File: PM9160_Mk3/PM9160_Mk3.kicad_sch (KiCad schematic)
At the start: 87 parts, among them J1 Conn_Coaxial, U1 BGA2869, U2 ATtiny416-M, U3 SY100EL33L, U4 SY100EL33L, U5 LM317L_TO92

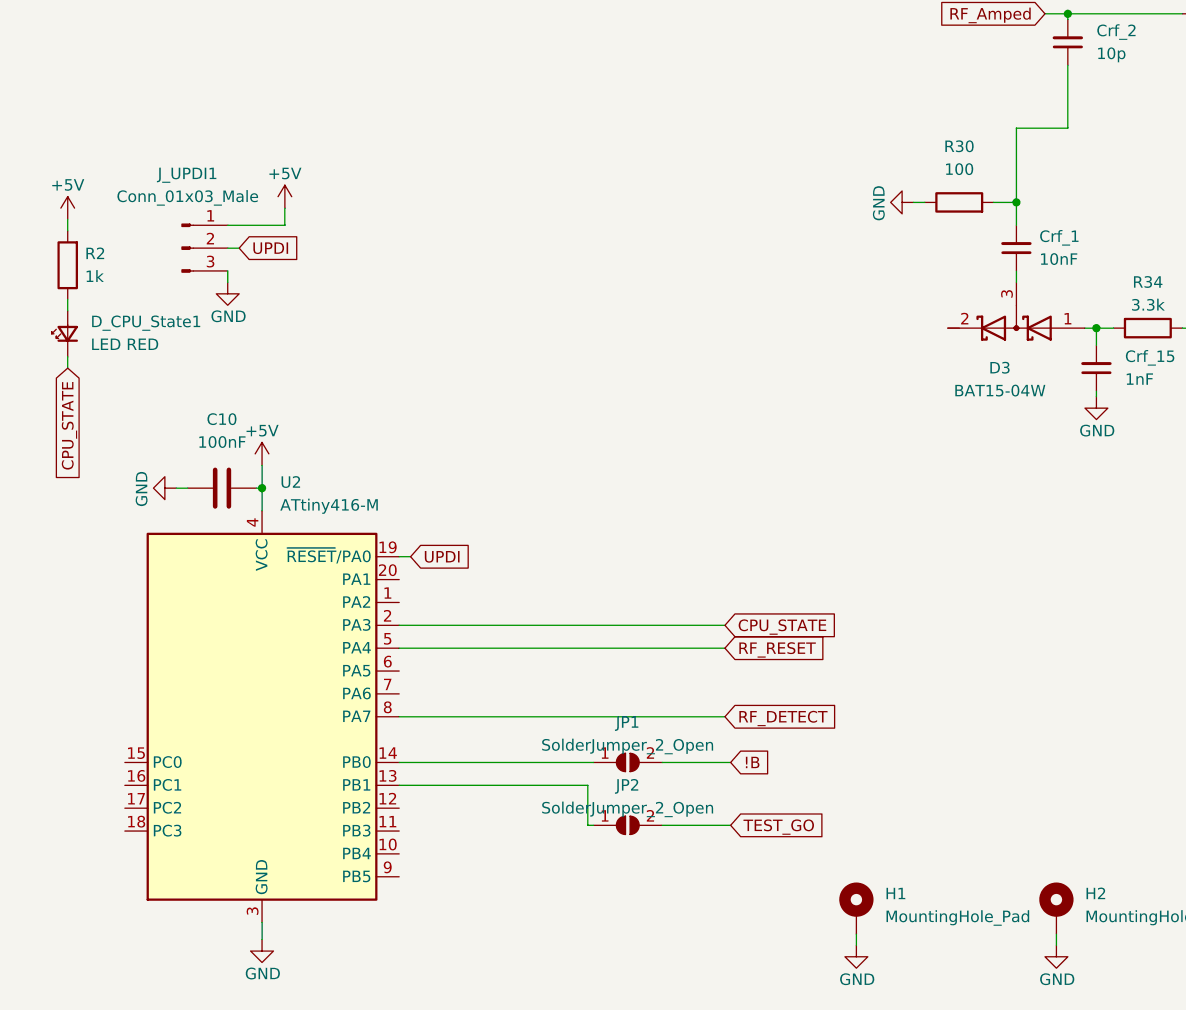
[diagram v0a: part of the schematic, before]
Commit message: CPU change and fixed via clearances
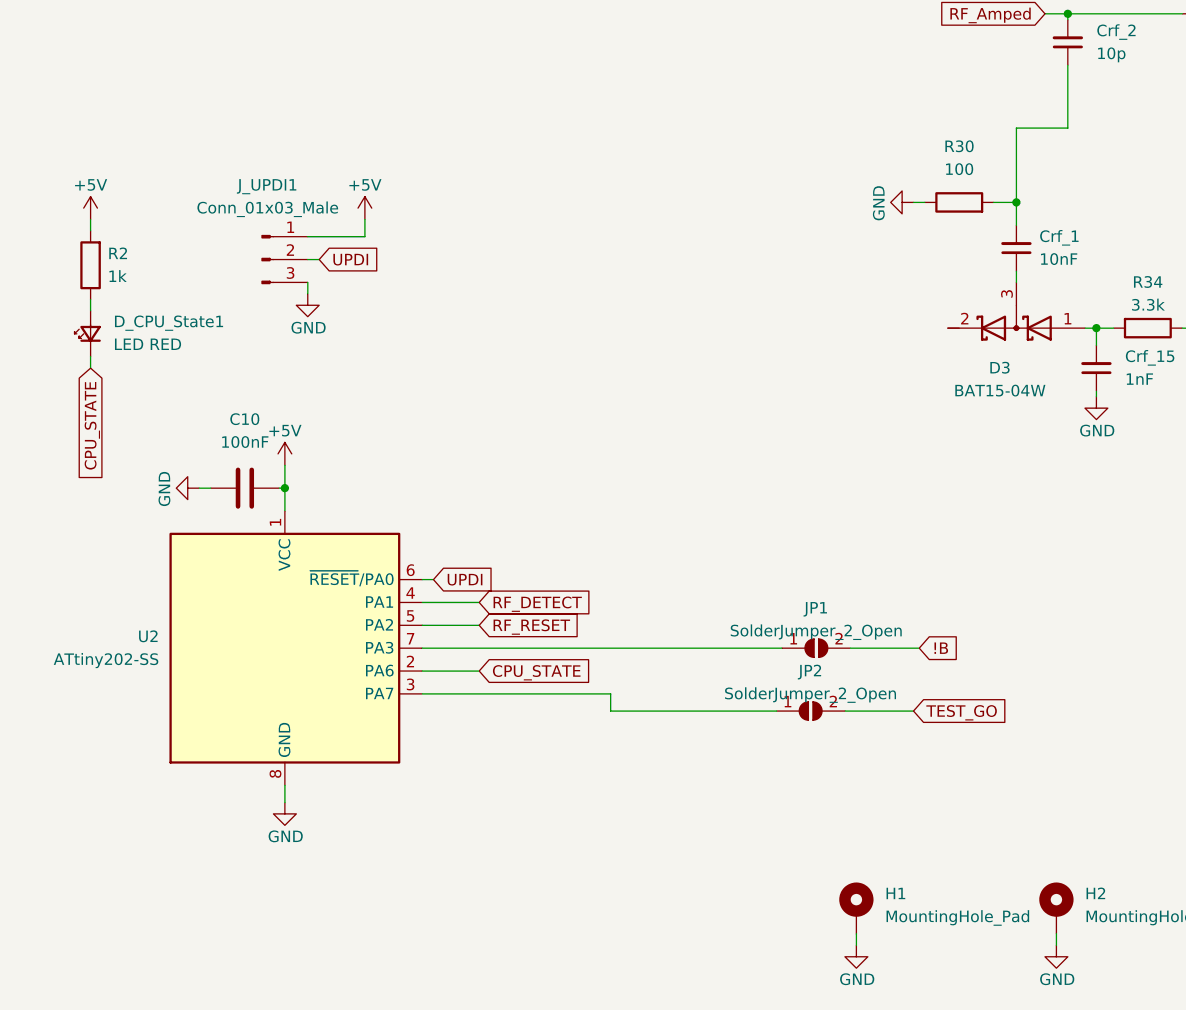
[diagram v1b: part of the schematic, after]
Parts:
- removed U2: ATtiny416-M, Package_DFN_QFN:VQFN-20-1EP_3x3mm_P0.4mm_EP1.7x1.7mm, symbol MCU_Microchip_ATtiny:ATtiny416-M
- added U2: ATtiny202-SS, Package_SO:SOIC-8_3.9x4.9mm_P1.27mm, symbol MCU_Microchip_ATtiny:ATtiny202-SS
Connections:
- net +5V: now also U2.1 (VCC)
- net CPU_STATE: now also U2.2 (PA6)
- net GND: now also U2.8 (GND)
- net RF_DETECT: now also U2.4 (PA1)
- net RF_RESET: now also U2.5 (PA2)
- net UPDI: now also U2.6 (~{RESET}/PA0)
- net at JP1.1 (A): now also U2.7 (PA3)
- net at JP2.1 (A): now also U2.3 (PA7)
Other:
- moved on the sheet: C10, D_CPU_State1, JP1, JP2, J_UPDI1, R2
